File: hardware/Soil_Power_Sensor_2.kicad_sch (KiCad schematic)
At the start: 48 parts, among them J1 Conn_01x02, J2 DC050-T, Q10 AO3401A, Q8 AO3401A, Q9 BSS123, U1 BQ24210DQCR, U11 TPS631000DRLR

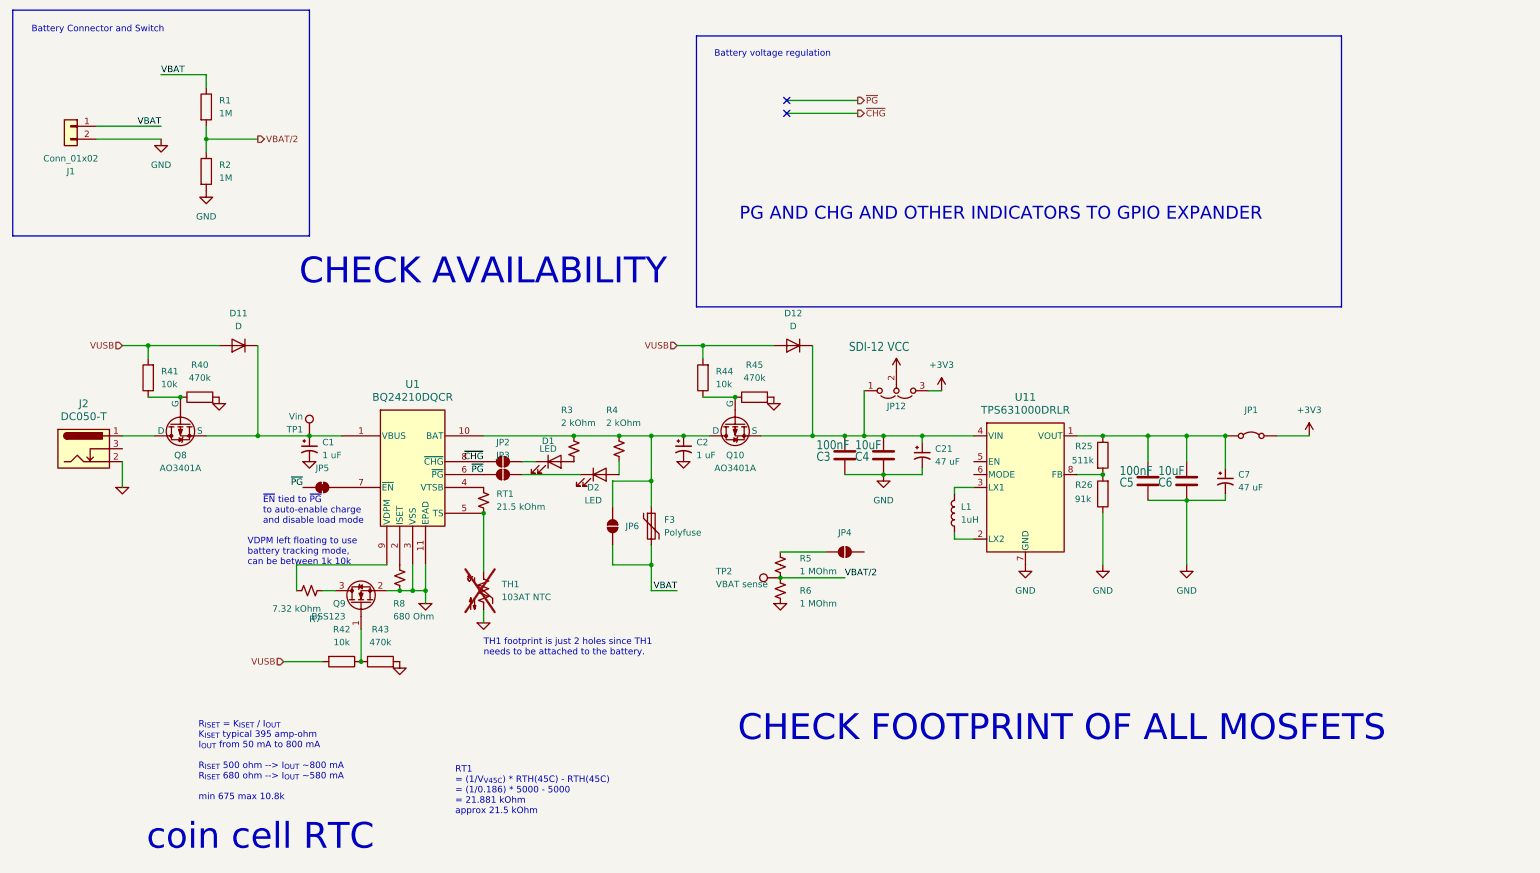
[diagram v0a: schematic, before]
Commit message: pin numbering and changed mosfets
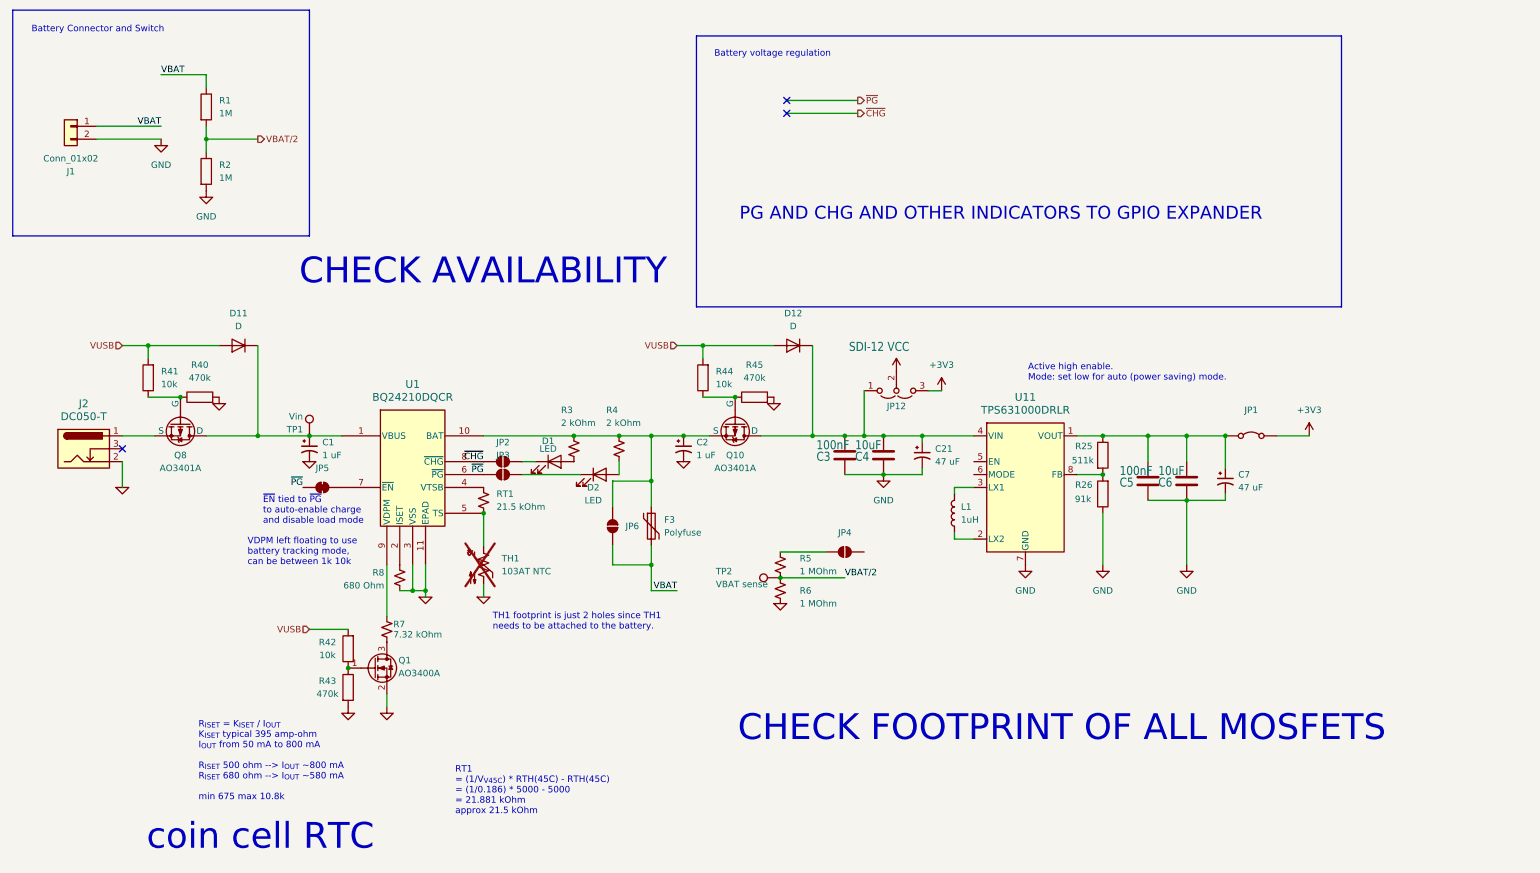
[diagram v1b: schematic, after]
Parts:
- removed Q9: BSS123, Package_TO_SOT_SMD:SOT-23, symbol Transistor_FET:BSS123
- added Q1: AO3400A, Package_TO_SOT_SMD:SOT-23, symbol Transistor_FET:AO3400A
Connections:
- net GND: now also Q1.2 (S)
- net at C2.1, F3.1, JP6.2 (B)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: now also Q10.3 (S); no longer Q10.1 (D)
- net at C21.1, C3.1, C4.1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: now also Q10.1 (D); no longer Q10.3 (S)
- net at J2.1: now also Q8.3 (S); no longer Q8.1 (D)
- net at C1.1, D11.1 (K), TP1.1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: now also Q8.1 (D); no longer Q8.3 (S)
- net at R42.1, R43.1: now also Q1.1 (G)
- net at R7.2: now also Q1.3 (D)
- no-connect marks 2 -> 3
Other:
- note added: "Active high enable. Mode: set low for auto (power saving) mode."
- moved on the sheet: Q10, Q8, R42, R43, R7, TH1

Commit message: lower power buck-boost
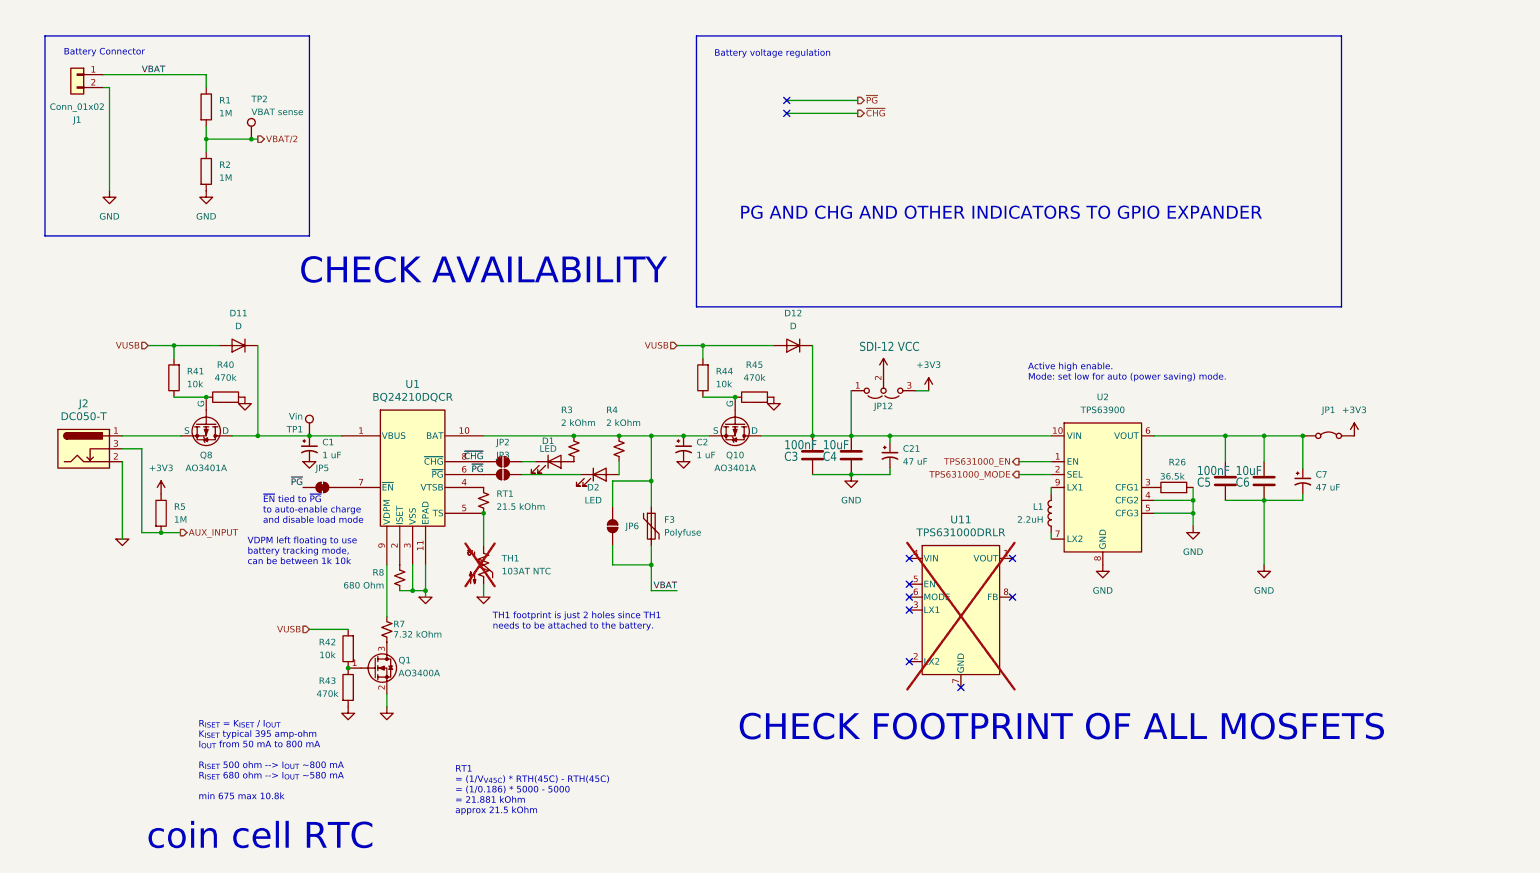
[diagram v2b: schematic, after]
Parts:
- removed JP4: SolderJumper_2_Open, Jumper:SolderJumper-2_P1.3mm_Open_RoundedPad1.0x1.5mm, symbol Jumper:SolderJumper_2_Open
- removed R25: 511k, Resistor_SMD:R_0603_1608Metri, symbol Device:R
- removed R5, R6: 1 MOhm, Resistor_SMD:R_0603_1608Metric, symbol Device:R_Small_US
- added R5: 1M, Resistor_SMD:R_0603_1608Metric, symbol Device:R
- added U2: TPS63900, Package_SON:WSON-10-1EP_2.5x2.5mm_P0.5mm_EP1.2x2mm_ThermalVias, symbol Regulator_Switching:TPS63900
- L1: value 1uH -> 2.2uH
- R26: value 91k -> 36.5k
- U11: now not fitted; now left out of the parts list
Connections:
- net +3V3: now also R5.1
- net GND: now also R26.2, U2.11 (GND), U2.4 (CFG2), U2.5 (CFG3), U2.8 (GND); no longer R26.1, U11.7 (GND)
- net at C21.1, C3.1, C4.1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: now also U2.10 (VIN); no longer U11.4 (VIN)
- net at C5.1, C6.1, C7.1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: now also U2.6 (VOUT); no longer U11.1 (VOUT)
- net AUX_INPUT: now reaches J2.3
- net AUX_INPUT: now also R5.2
- net at U11.8 (FB): no longer R26.2
- net at L1.1: now also U2.9 (LX1); no longer U11.3 (LX1)
- net at L1.2: now also U2.7 (LX2); no longer U11.2 (LX2)
- new net: R26.1, U2.3 (CFG1)
- new net TPS631000_EN: U2.1 (EN)
- new net TPS631000_MODE: U2.2 (SEL)
- no-connect marks 3 -> 10
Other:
- note added: "Battery Connector"
- note removed: "Battery Connector and Switch"
- moved on the sheet: C21, C3, C4, C5, C6, C7, J1, JP1, JP12, L1, Q8, R26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

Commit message: rough layout spacing
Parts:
- removed D11, D12: D, Diode_SMD:D_0603_1608Metric, symbol Device:D
- removed F3: Polyfuse, Fuse:Fuse_0603_1608Metric, symbol Device:Polyfuse
- removed JP6: SolderJumper_2_Open, Jumper:SolderJumper-2_P1.3mm_Open_RoundedPad1.0x1.5mm, symbol Jumper:SolderJumper_2_Open
- removed R42, R44: 10k, Resistor_SMD:R_0603_1608Metric, symbol Device:R
- removed R43, R45: 470k, Resistor_SMD:R_0603_1608Metric, symbol Device:R
- added D1, D2: RB521S-40, Diode_SMD:D_SOD-523, symbol Device:D_Schottky
- added JP1, JP2, JP8, JP9: SolderJumper_2_Open, Jumper:SolderJumper-2_P1.3mm_Open_RoundedPad1.0x1.5mm, symbol Jumper:SolderJumper_2_Open
- added R2, R3: 470k, Resistor_SMD:R_0603_1608Metric, symbol Device:R
- BT1: renamed from J1; value Conn_01x02 -> Battery_Cell; symbol Connector_Generic:Conn_01x02 -> Device:Battery_Cell
- C1, C2: value 1 uF -> 1uF; symbol Device:C_Polarized_Small_US -> Device:C
- C3: value 100nF -> 0.1uF
- C5: renamed from C21; value 47 uF -> 47uF
- C6: renamed from C5; value 100nF -> 0.1uF
- C8: renamed from C7; value 47 uF -> 47uF
- JP3: renamed from JP12; value Jumper_3_Open -> SolderJumper_3_Open; symbol Jumper:Jumper_3_Open -> Jumper:SolderJumper_3_Open
- Q1: renamed from Q8; symbol Simulation_SPICE:PMOS -> Transistor_FET:AO3401A
- Q2: renamed from Q10; symbol Simulation_SPICE:PMOS -> Transistor_FET:AO3401A
- R12: renamed from R8; value 680 Ohm -> 680; symbol Device:R_Small_US -> Device:R
- R13: renamed from R7; value 7.32 kOhm -> 7.32k; symbol Device:R_Small_US -> Device:R
- R5: renamed from R3; value 2 kOhm -> 2k; symbol Device:R_Small_US -> Device:R
- R6: renamed from R4; value 2 kOhm -> 2k; symbol Device:R_Small_US -> Device:R
- R7: renamed from R5; value 1M -> 470k
- R9: renamed from RT1; value 21.5 kOhm -> 21.5k; symbol Device:R_Small_US -> Device:R
- TH1: symbol Device:Thermistor_NTC_US -> Device:Thermistor_NTC; now fitted
- TP1: value Vin -> V_{BUS}
- TP2: value VBAT sense -> V_{BAT}/2
- U1: footprint BQ24210:DQC10_P84X2P4 -> Package_SON:WSON-10-1EP_2x3mm_P0.5mm_EP0.84x2.4mm_ThermalVias; symbol BQ24210:BQ24210DQCR -> Soil Power Sensor-eagle-import:BQ24210DQCR
- renumbered C6 to C7, D1 to D3, D2 to D4, J2 to J1, JP1 to JP4, JP2 to JP5, JP5 to JP6, JP3 to JP7, Q1 to Q3, R41 to R1, R1 to R10, R2 to R11, R40 to R4, R26 to R8, U11 to U3
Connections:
- net 0 is gone; now on net GND: C1.2, C2.2, J1.2, R12.2, TH1.2, U1.11 (EPAD), U1.3 (VSS)
- net +3V3: now also R2.1, R3.1
- net GND: now also Q3.3 (D); no longer Q3.2 (S)
- net VUSB: now also R1.1, D1.2 (A), D2.2 (A); no longer R1.2
- net ~{CHG}: now also JP2.1 (A)
- net ~{PG}: now also JP1.1 (A)
- net at C2.1, Q2.3 (D), R5.1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: now also BT1.1 (+), JP8.1 (A)
- net at C3.1, C4.1, C5.1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: now also Q2.2 (S), D2.1 (K); no longer Q2.1 (D)
- net VUSB_MUX: now reaches Q3.1 (G)
- net VUSB_MUX: now also Q1.1 (G), Q2.1 (G), R1.2, R4.1
- net at R13.2: now also Q3.2 (S); no longer Q3.3 (D)
- net at C1.1, TP1.1, U1.1 (VBUS): now also Q1.2 (S), D1.1 (K); no longer Q1.1 (D)
- net AUX_INPUT: no longer names the net of R7.2
- net AUX_INPUT: now also JP9.2 (B); no longer J1.3
- net VBAT: no longer names the net of R10.1
- net VBAT: now also JP8.2 (B); no longer BT1.1 (Pin_1)
- new net: JP1.2 (B), R2.2
- new net: JP2.2 (B), R3.2
- new net SOLAR_DETECT: J1.3, JP9.1 (A)
- no-connect marks 10 -> 8
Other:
- note added: "Battery Charger"
- note added: "In typical operation, with both inputs connected, V_{solar} < V_{USB}. (Usually indoors when using USB input.) With V_{USB}=5 V, if V_{solar} > V_{USB}, then V_{bus} = V_{solar} rather than V_{USB}."
- note added: "It is possible for SDI-12 VCC to be as low as 3.0 V (low battery, no USB). To fix: auto select highest available voltage (not to exceed 5.5 V) with ideal ORing diode or power mux."
- note added: "R_{ISET} = K_{ISET} / I_{OUT} K_{ISET} is typically 395 amp-ohm I_{OUT} ranges from 50 mA to 800 mA R_{ISET}=500 ohm --> I_{OUT}~=800 mA R_{ISET}=680 ohm --> I_{OUT}~=580 mA min 675 max 10.8k"
- note added: "Recommended solar panel V_{OC}=6 V (max 18 V input)"
- note added: "VDPM left floating to use battery tracking mode, can be between 1k 10k. 7.32 kOhm enabled with USB."
- note added: "Voltage Regulation"
- note added: "coin cell RTC?"
- note removed: "Battery Connector"
- note removed: "Battery voltage regulation"
- note removed: "CHECK AVAILABILITY"
- note removed: "CHECK FOOTPRINT OF ALL MOSFETS"
- note removed: "PG AND CHG AND OTHER INDICATORS TO GPIO EXPANDER"
- note removed: "R_{ISET} = K_{ISET} / I_{OUT} K_{ISET} typical 395 amp-ohm I_{OUT} from 50 mA to 800 mA R_{ISET} 500 ohm --> I_{OUT} ~800 mA R_{ISET} 680 ohm --> I_{OUT} ~580 mA min 675 max 10.8k"
- note removed: "TH1 footprint is just 2 holes since TH1 needs to be attached to the battery."
- note removed: "VDPM left floating to use battery tracking mode, can be between 1k 10k"
- note removed: "coin cell RTC"
- moved on the sheet: C3, C4, C5, C6, C7, C8, D3, D4, J1, JP4, JP5, JP6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

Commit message: PCB layout with silkscreen annotations
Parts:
- removed JP6: SolderJumper_2_Bridged, Jumper:SolderJumper-2_P1.3mm_Bridged_RoundedPad1.0x1.5mm, symbol Jumper:SolderJumper_2_Bridged
- renumbered JP7 to JP6, JP8 to JP7, JP9 to JP8
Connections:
- net ~{PG}: now also U1.7 (~{EN})
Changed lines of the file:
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@@
 	(wire
 		(pts
+			(xy 64.77 46.99) (xy 72.39 46.99)
+		)
+		(stroke
+			(width 0)
+			(type default)
+		)
+	)
+	(wire
+		(pts
 			(xy 45.72 31.75) (xy 45.72 25.4)
 		)
@@
 	)
 	(symbol
-		(lib_id "Jumper:SolderJumper_2_Bridged")
-		(at 68.58 46.99 0)
-		(unit 1)
-		(exclude_from_sim no)
-		(in_bom yes)
-		(on_board yes)
-		(dnp no)
-		(property "Reference" "JP6"
-			(at 68.58 44.958 0)
-			(effects
-				(font
-					(size 1.27 1.27)
-				)
-			)
-		)
-		(property "Value" "SolderJumper_2_Bridged"
-			(at 68.58 43.18 0)
-			(effects
-				(font
-					(size 1.27 1.27)
-				)
-				(hide yes)
-			)
-		)
-		(property "Footprint" "Jumper:SolderJumper-2_P1.3mm_Bridged_RoundedPad1.0x1.5mm"
-			(at 68.58 46.99 0)
-			(effects
-				(font
-					(size 1.27 1.27)
-				)
-				(hide yes)
-			)
-		)
-		(property "Datasheet" "~"
-			(at 68.58 46.99 0)
-			(effects
-				(font
-					(size 1.27 1.27)
-				)
-				(hide yes)
-			)
-		)
-		(property "Description" "Solder Jumper, 2-pole, closed/bridged"
-			(at 68.58 46.99 0)
-			(effects
-				(font
-					(size 1.27 1.27)
-				)
-				(hide yes)
-			)
-		)
-		(property "MFC" ""
-			(at 68.58 46.99 0)
-			(effects
-				(font
-					(size 1.27 1.27)
-				)
-				(hide yes)
-			)
-		)
-		(property "MPN" ""
-			(at 68.58 46.99 0)
-			(effects
-				(font
-					(size 1.27 1.27)
-				)
-				(hide yes)
-			)
-		)
-		(property "QTY" ""
-			(at 68.58 46.99 0)
-			(effects
-				(font
-					(size 1.27 1.27)
-				)
-				(hide yes)
-			)
-		)
-		(property "REF" ""
-			(at 68.58 46.99 0)
-			(effects
-				(font
-					(size 1.27 1.27)
-				)
-				(hide yes)
-			)
-		)
-		(property "SNAPEDA_PACKAGE_ID" ""
-			(at 68.58 46.99 0)
-			(effects
-				(font
-					(size 1.27 1.27)
-				)
-				(hide yes)
-			)
-		)
-		(property "Digikey" ""
-			(at 68.58 46.99 0)
-			(effects
-				(font
-					(size 1.27 1.27)
-				)
-				(hide yes)
-			)
-		)
-		(pin "1"
-		)
-		(pin "2"
-		)
-		(instances
-			(project "Soil Power Sensor"
-				(path "/5300ec4d-4648-40a1-8d89-4fa6b3bf32a3/642281e5-1644-4dc3-b6e5-bcf5b1c03ff1"
-					(reference "JP6")
-					(unit 1)
-				)
-			)
-		)
-	)
-	(symbol
 		(lib_id "Device:R")
 		(at 138.43 59.69 0)
@@
 		(dnp no)
 		(fields_autoplaced yes)
-		(property "Reference" "JP7"
+		(property "Reference" "JP6"
 			(at 106.68 50.8 0)
 			(effects
@@
 			(project "Soil Power Sensor"
 				(path "/5300ec4d-4648-40a1-8d89-4fa6b3bf32a3/642281e5-1644-4dc3-b6e5-bcf5b1c03ff1"
-					(reference "JP7")
+					(reference "JP6")
 					(unit 1)
 				)
@@
 		(dnp no)
 		(fields_autoplaced yes)
-		(property "Reference" "JP9"
+		(property "Reference" "JP8"
 			(at 39.37 57.1499 90)
 			(effects
@@
 			(project "Soil Power Sensor"
 				(path "/5300ec4d-4648-40a1-8d89-4fa6b3bf32a3/642281e5-1644-4dc3-b6e5-bcf5b1c03ff1"
-					(reference "JP9")
+					(reference "JP8")
 					(unit 1)
 				)
@@
 		(dnp no)
 		(fields_autoplaced yes)
-		(property "Reference" "JP8"
+		(property "Reference" "JP7"
 			(at 133.35 52.07 0)
 			(effects
@@
 			(project "Soil Power Sensor"
 				(path "/5300ec4d-4648-40a1-8d89-4fa6b3bf32a3/642281e5-1644-4dc3-b6e5-bcf5b1c03ff1"
-					(reference "JP8")
+					(reference "JP7")
 					(unit 1)
 				)

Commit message: finishing touches and fabrication output
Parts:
- added J2: ~, Connector_JST:JST_PH_S2B-PH-SM4-TB_1x02-1MP_P2.00mm_Horizontal, symbol Connector_Generic_MountingPin:Conn_01x02_MountingPin
- BT1: footprint Connector_JST:JST_PH_S2B-PH-K_1x02_P2.00mm_Horizontal -> Connector_PinHeader_2.54mm:PinHeader_1x02_P2.54mm_Vertical; now not fitted; now left out of the parts list
- C3, C6: value 0.1uF -> 100nF; MPN CC0603KRX5R5BB106 -> (none)
- C4, C7: MPN CC0603KRX5R5BB106 -> (none)
- C5, C8: footprint Capacitor_SMD:C_0603_1608Metric -> Capacitor_SMD:C_0805_2012Metric
- D1, D2: value RB521S-40 -> RB160M-30; footprint Diode_SMD:D_SOD-523 -> Diode_SMD:D_SOD-123; LCSC C7502703 -> C7502715
- D3, D4: LCSC (none) -> C2286; MPN (none) -> KT-0603R
- J1: footprint Connector_BarrelJack:BarrelJack_Horizontal -> Connector_BarrelJack:BarrelJack_Wuerth_694106106102_2.0x5.5mm; REF J1 -> (none)
- JP1, JP2, JP8, TP1, TP2: now left out of the parts list
- JP3: value SolderJumper_3_Open -> SolderJumper_3_Bridged12; symbol Jumper:SolderJumper_3_Open -> Jumper:SolderJumper_3_Bridged12; LCSC (none) -> C2937625; now in the parts list
- JP4: LCSC (none) -> C492401
- JP5, JP6, JP7: value SolderJumper_2_Open -> SolderJumper_2_Bridged; symbol Jumper:SolderJumper_2_Open -> Jumper:SolderJumper_2_Bridged; now left out of the parts list
- L1: LCSC (none) -> C1043; MPN (none) -> CMI201209U2R2KT
- Q1, Q2: LCSC (none) -> C15127; MFC (none) -> Alpha Omega Semicon; MPN (none) -> AO3401A
- Q3: LCSC (none) -> C20917; MFC (none) -> Alpha Omega Semicon; MPN (none) -> AO3400A
- R1, R4: LCSC C114670 -> (none); MPN RC0603FR-07510RL -> (none)
- R10: renamed from R12; value 680 -> 680R
- TH1: REF TH1 -> (none)
- U1: REF U1 -> (none)
- renumbered R13 to R11, R10 to R12, R11 to R13
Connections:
- net TPS631000_EN is gone; now on an unnamed net: U2.1 (EN)
- net TPS631000_MODE is gone; now on an unnamed net: U2.2 (SEL)
- net GND: now also J2.2 (Pin_2), J2.MP (MountPin)
- net at BT1.1 (+), C2.1, JP7.1 (A)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: now also J2.1 (Pin_1)
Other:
- note removed: "coin cell RTC?"
- moved on the sheet: R12, R13, TP2
